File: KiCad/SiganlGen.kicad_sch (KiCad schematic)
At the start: 1 part, among them J1 Barrel_Jack_MountingPin

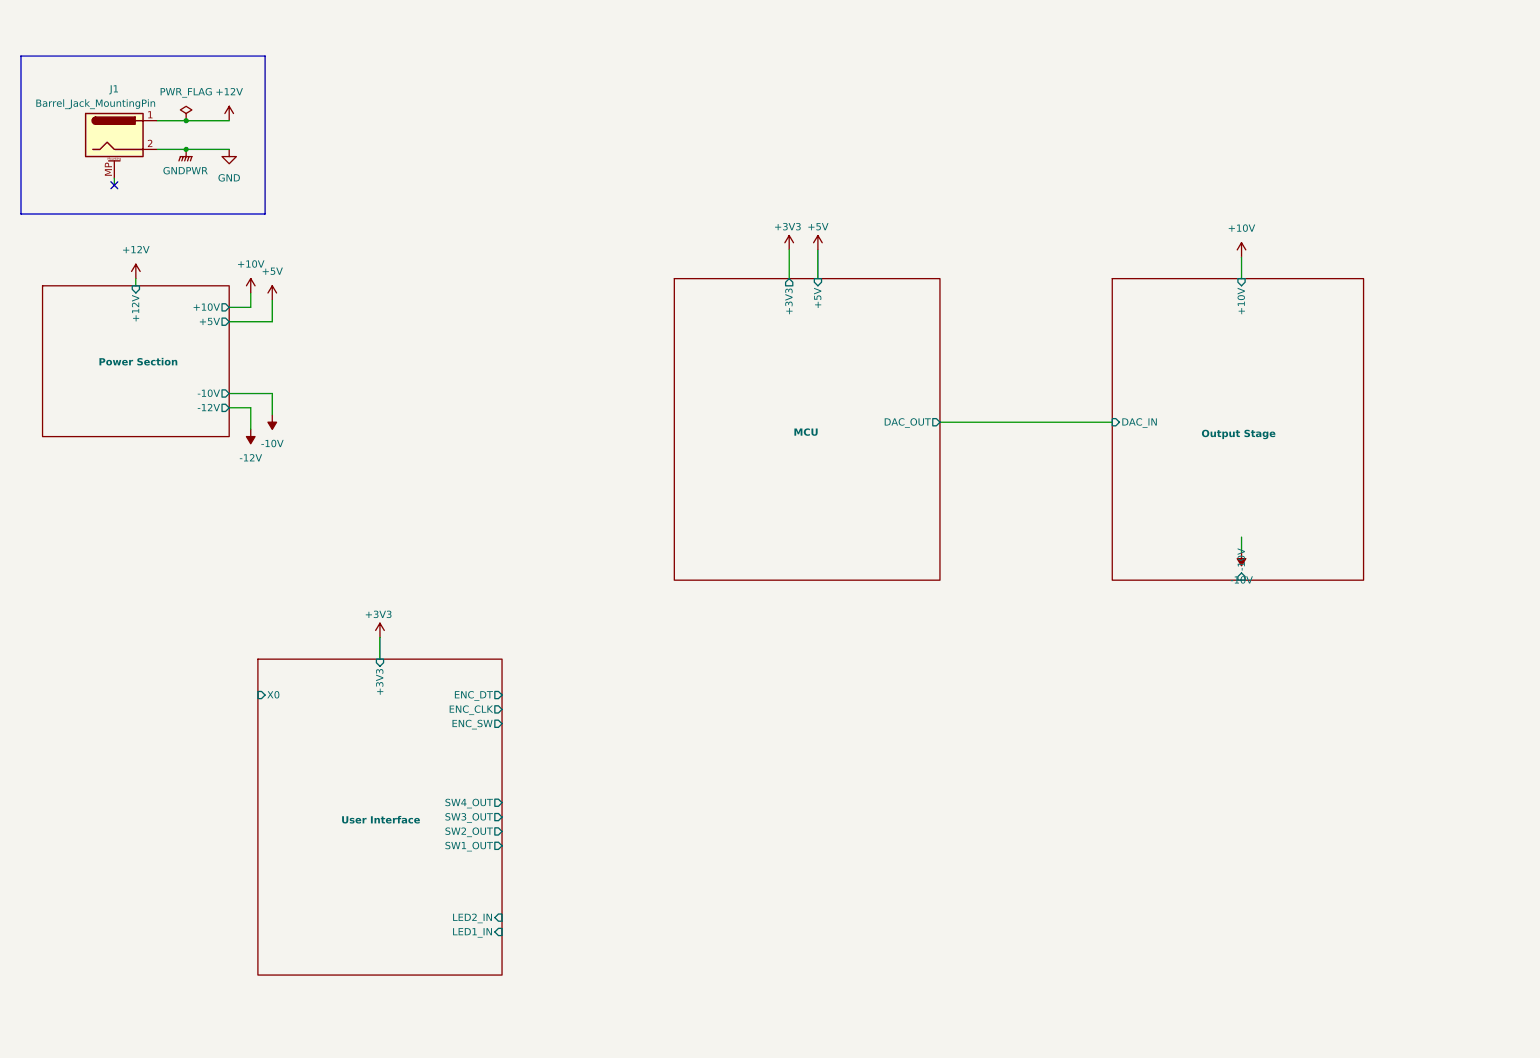
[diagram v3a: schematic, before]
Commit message: UI connections to uC
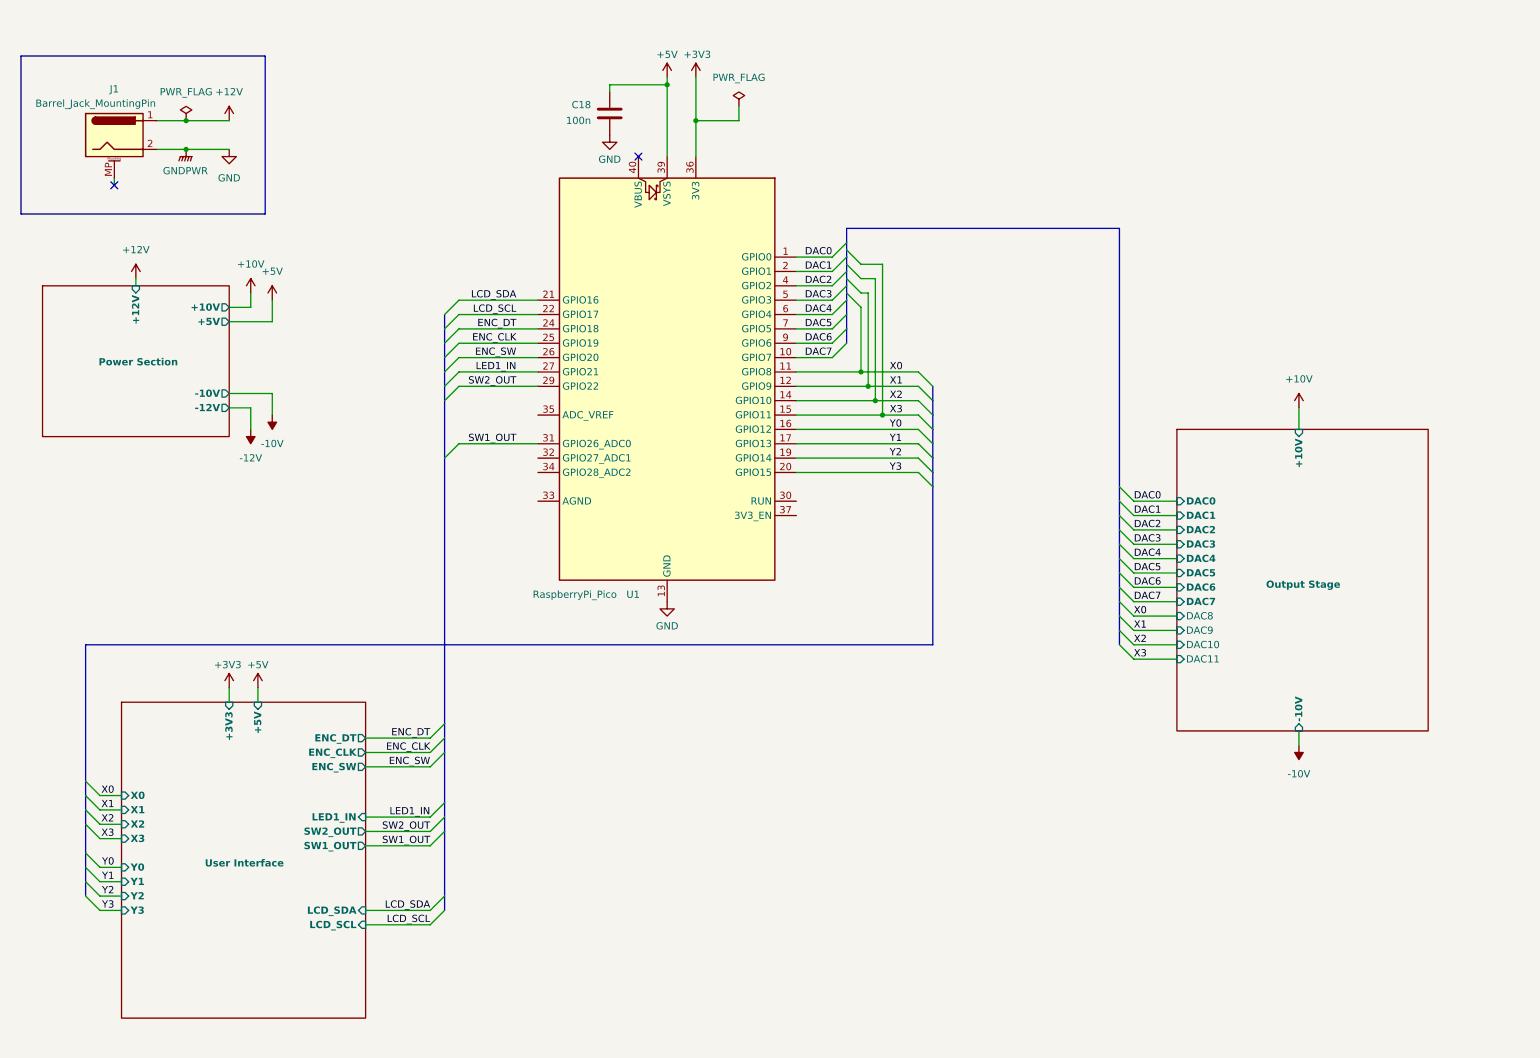
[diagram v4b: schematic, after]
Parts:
- added C18: 100n, Capacitor_SMD:C_0805_2012Metric_Pad1.18x1.45mm_HandSolder, symbol Device:C
- added U1: RaspberryPi_Pico, Module_RaspberryPi_Pico:RaspberryPi_Pico_Common, symbol MCU_Module_RaspberryPi_Pico:RaspberryPi_Pico
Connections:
- net +3V3: now also U1.36 (3V3)
- net +5V: now also C18.1, U1.39 (VSYS)
- net GND: now also C18.2, U1.13 (GND), U1.18 (GND), U1.23 (GND), U1.28 (GND), U1.3 (GND), U1.38 (GND), U1.8 (GND)
- new net DAC0: U1.1 (GPIO0)
- new net DAC1: U1.2 (GPIO1)
- new net DAC2: U1.4 (GPIO2)
- new net DAC3: U1.5 (GPIO3)
- new net DAC4: U1.6 (GPIO4)
- new net DAC5: U1.7 (GPIO5)
- new net DAC6: U1.9 (GPIO6)
- new net DAC7: U1.10 (GPIO7)
- new net ENC_CLK: U1.25 (GPIO19)
- new net ENC_DT: U1.24 (GPIO18)
- new net ENC_SW: U1.26 (GPIO20)
- new net LCD_SCL: U1.22 (GPIO17)
- new net LCD_SDA: U1.21 (GPIO16)
- new net LED1_IN: U1.27 (GPIO21)
- new net SW1_OUT: U1.31 (GPIO26_ADC0)
- new net SW2_OUT: U1.29 (GPIO22)
- new net X0: U1.11 (GPIO8)
- new net X1: U1.12 (GPIO9)
- new net X2: U1.14 (GPIO10)
- new net X3: U1.15 (GPIO11)
- new net Y0: U1.16 (GPIO12)
- new net Y1: U1.17 (GPIO13)
- new net Y2: U1.19 (GPIO14)
- new net Y3: U1.20 (GPIO15)
- no-connect marks 1 -> 2
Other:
- removed sheet MCU
- sheet Output Stage ports: added DAC0, DAC1, DAC10, DAC11, DAC2, DAC3, DAC4, DAC5, DAC6, DAC7, DAC8, DAC9; removed DAC_IN
- sheet User Interface ports: added +5V, LCD_SCL, LCD_SDA, X1, X2, X3, Y0, Y1, Y2, Y3; removed LED2_IN, SW3_OUT, SW4_OUT

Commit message: First DAC layout, rough board layout
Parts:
- renumbered C18 to C1
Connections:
- net GND: now also J1.MP (MountPin)
- no-connect marks 2 -> 1
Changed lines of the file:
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@@
 	)
 	(junction
+		(at 40.64 36.83)
+		(diameter 0)
+		(color 0 0 0 0)
+	)
+	(junction
 		(at 45.72 36.83)
 		(diameter 0)
@@
 		(at 125.73 38.1)
 	)
-	(no_connect
-		(at 33.02 43.18)
-	)
 	(bus_entry
 		(at 162.56 62.23)
@@
 	(wire
 		(pts
+			(xy 33.02 43.18) (xy 33.02 41.91)
+		)
+		(stroke
+			(width 0)
+			(type default)
+		)
+	)
+	(wire
+		(pts
 			(xy 213.36 124.46) (xy 220.98 124.46)
 		)
@@
 		)
 	)
-	(wire
-		(pts
-			(xy 33.02 43.18) (xy 33.02 41.91)
-		)
-		(stroke
-			(width 0)
-			(type default)
-		)
-	)
 	(bus
 		(pts
@@
 	(wire
 		(pts
+			(xy 40.64 36.83) (xy 40.64 43.18)
+		)
+		(stroke
+			(width 0)
+			(type default)
+		)
+	)
+	(wire
+		(pts
 			(xy 166.37 78.74) (xy 175.26 78.74)
 		)
@@
 	(wire
 		(pts
+			(xy 33.02 43.18) (xy 40.64 43.18)
+		)
+		(stroke
+			(width 0)
+			(type default)
+		)
+	)
+	(wire
+		(pts
 			(xy 213.36 104.14) (xy 220.98 104.14)
 		)
@@
 		(dnp no)
 		(fields_autoplaced yes)
-		(property "Reference" "#PWR05"
+		(property "Reference" "#PWR018"
 			(at 60.96 67.31 0)
 			(effects
@@
 			(project "SiganlGen"
 				(path "/e2db369b-fed9-4358-b449-15db5155edf2"
-					(reference "#PWR05")
+					(reference "#PWR018")
 					(unit 1)
 				)
@@
 		(dnp no)
 		(fields_autoplaced yes)
-		(property "Reference" "#PWR03"
+		(property "Reference" "#PWR02"
 			(at 45.72 41.91 0)
 			(effects
@@
 			(project "SiganlGen"
 				(path "/e2db369b-fed9-4358-b449-15db5155edf2"
-					(reference "#PWR03")
+					(reference "#PWR02")
 					(unit 1)
 				)
@@
 		(dnp no)
 		(fields_autoplaced yes)
-		(property "Reference" "#PWR04"
+		(property "Reference" "#PWR06"
 			(at 57.15 66.04 0)
 			(effects
@@
 			(project "SiganlGen"
 				(path "/e2db369b-fed9-4358-b449-15db5155edf2"
-					(reference "#PWR04")
+					(reference "#PWR06")
 					(unit 1)
 				)
@@
 		(on_board yes)
 		(dnp no)
-		(property "Reference" "#PWR032"
+		(property "Reference" "#PWR028"
 			(at 135.89 27.94 0)
 			(effects
@@
 			(project "SiganlGen"
 				(path "/e2db369b-fed9-4358-b449-15db5155edf2"
-					(reference "#PWR032")
+					(reference "#PWR028")
 					(unit 1)
 				)
@@
 		(dnp no)
 		(fields_autoplaced yes)
-		(property "Reference" "#PWR010"
+		(property "Reference" "#PWR020"
 			(at 60.96 80.01 0)
 			(effects
@@
 			(project "SiganlGen"
 				(path "/e2db369b-fed9-4358-b449-15db5155edf2"
-					(reference "#PWR010")
+					(reference "#PWR020")
 					(unit 1)
 				)
@@
 		(dnp no)
 		(fields_autoplaced yes)
-		(property "Reference" "#PWR022"
+		(property "Reference" "#PWR01"
 			(at 36.83 63.5 0)
 			(effects
@@
 			(project "SiganlGen"
 				(path "/e2db369b-fed9-4358-b449-15db5155edf2"
-					(reference "#PWR022")
+					(reference "#PWR01")
 					(unit 1)
 				)
@@
 		(dnp no)
 		(fields_autoplaced yes)
-		(property "Reference" "#PWR01"
+		(property "Reference" "#PWR03"
 			(at 53.34 35.56 0)
 			(effects
@@
 			(project "SiganlGen"
 				(path "/e2db369b-fed9-4358-b449-15db5155edf2"
-					(reference "#PWR01")
+					(reference "#PWR03")
 					(unit 1)
 				)
@@
 		(on_board yes)
 		(dnp no)
-		(property "Reference" "#PWR023"
+		(property "Reference" "#PWR05"
 			(at 53.34 135.89 0)
 			(effects
@@
 			(project "SiganlGen"
 				(path "/e2db369b-fed9-4358-b449-15db5155edf2"
-					(reference "#PWR023")
+					(reference "#PWR05")
 					(unit 1)
 				)
@@
 		(on_board yes)
 		(dnp no)
-		(property "Reference" "#PWR033"
+		(property "Reference" "#PWR022"
 			(at 130.81 27.94 0)
 			(effects
@@
 			(project "SiganlGen"
 				(path "/e2db369b-fed9-4358-b449-15db5155edf2"
-					(reference "#PWR033")
+					(reference "#PWR022")
 					(unit 1)
 				)
@@
 		(on_board yes)
 		(dnp no)
-		(property "Reference" "#PWR020"
+		(property "Reference" "#PWR023"
 			(at 130.81 123.19 0)
 			(effects
@@
 			(project "SiganlGen"
 				(path "/e2db369b-fed9-4358-b449-15db5155edf2"
-					(reference "#PWR020")
+					(reference "#PWR023")
 					(unit 1)
 				)
@@
 		(dnp no)
 		(fields_autoplaced yes)
-		(property "Reference" "#PWR021"
+		(property "Reference" "#PWR030"
 			(at 242.57 86.36 0)
 			(effects
@@
 			(project "SiganlGen"
 				(path "/e2db369b-fed9-4358-b449-15db5155edf2"
-					(reference "#PWR021")
+					(reference "#PWR030")
 					(unit 1)
 				)
@@
 		(dnp no)
 		(fields_autoplaced yes)
-		(property "Reference" "#PWR018"
+		(property "Reference" "#PWR031"
 			(at 242.57 138.43 0)
 			(effects
@@
 			(project "SiganlGen"
 				(path "/e2db369b-fed9-4358-b449-15db5155edf2"
-					(reference "#PWR018")
+					(reference "#PWR031")
 					(unit 1)
 				)
@@
 		(on_board yes)
 		(dnp no)
-		(property "Reference" "#PWR011"
+		(property "Reference" "#PWR021"
 			(at 120.65 40.64 0)
 			(effects
@@
 			(project "SiganlGen"
 				(path "/e2db369b-fed9-4358-b449-15db5155edf2"
-					(reference "#PWR011")
+					(reference "#PWR021")
 					(unit 1)
 				)
@@
 		(dnp no)
 		(fields_autoplaced yes)
-		(property "Reference" "#PWR06"
+		(property "Reference" "#PWR010"
 			(at 57.15 82.55 0)
 			(effects
@@
 			(project "SiganlGen"
 				(path "/e2db369b-fed9-4358-b449-15db5155edf2"
-					(reference "#PWR06")
+					(reference "#PWR010")
 					(unit 1)
 				)
@@
 		(on_board yes)
 		(dnp no)
-		(property "Reference" "C18"
+		(property "Reference" "C1"
 			(at 117.348 28.956 0)
 			(effects
@@
 			(project "SiganlGen"
 				(path "/e2db369b-fed9-4358-b449-15db5155edf2"
-					(reference "C18")
+					(reference "C1")
 					(unit 1)
 				)
@@
 		(on_board yes)
 		(dnp no)
-		(property "Reference" "#PWR028"
+		(property "Reference" "#PWR011"
 			(at 58.42 135.89 0)
 			(effects
@@
 			(project "SiganlGen"
 				(path "/e2db369b-fed9-4358-b449-15db5155edf2"
-					(reference "#PWR028")
+					(reference "#PWR011")
 					(unit 1)
 				)
@@
 		(dnp no)
 		(fields_autoplaced yes)
-		(property "Reference" "#PWR02"
+		(property "Reference" "#PWR04"
 			(at 53.34 43.18 0)
 			(effects
@@
 			(project "SiganlGen"
 				(path "/e2db369b-fed9-4358-b449-15db5155edf2"
-					(reference "#PWR02")
+					(reference "#PWR04")
 					(unit 1)
 				)

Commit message: minor changes, testing
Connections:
- no-connect marks 1 -> 7

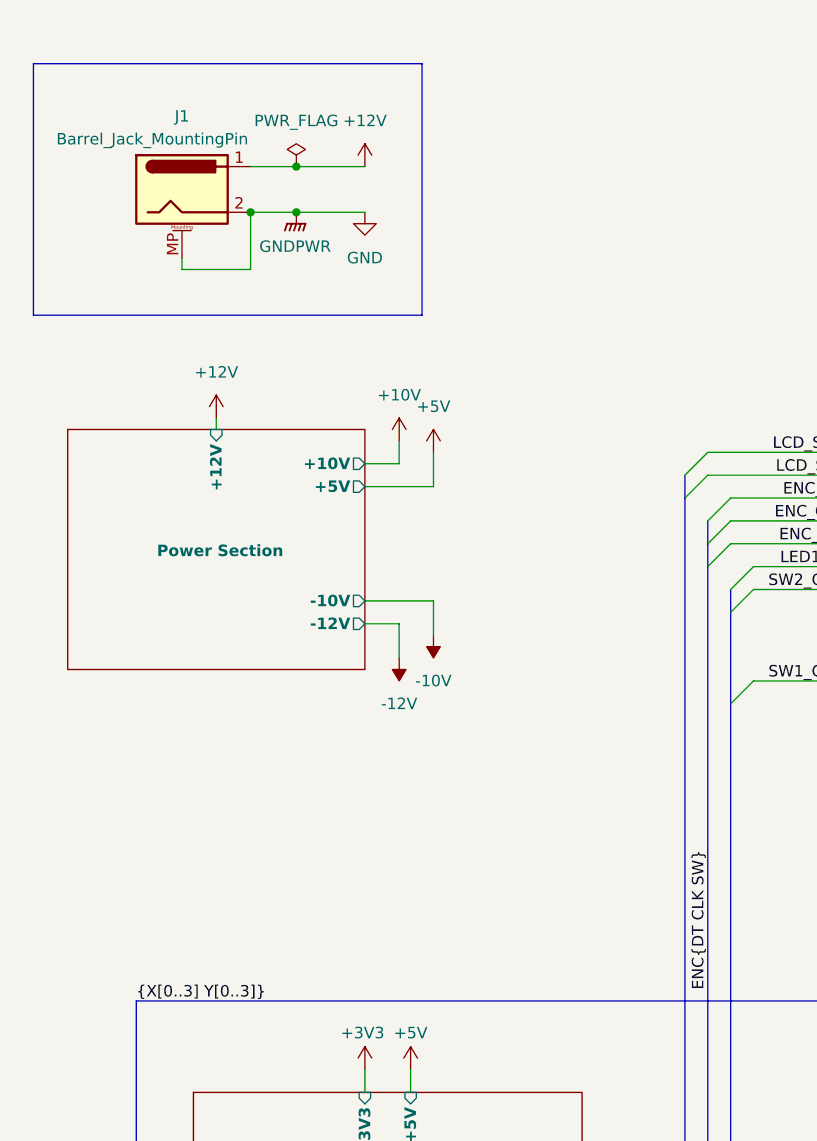
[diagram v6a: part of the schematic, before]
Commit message: Added protection elements and an additional input connector
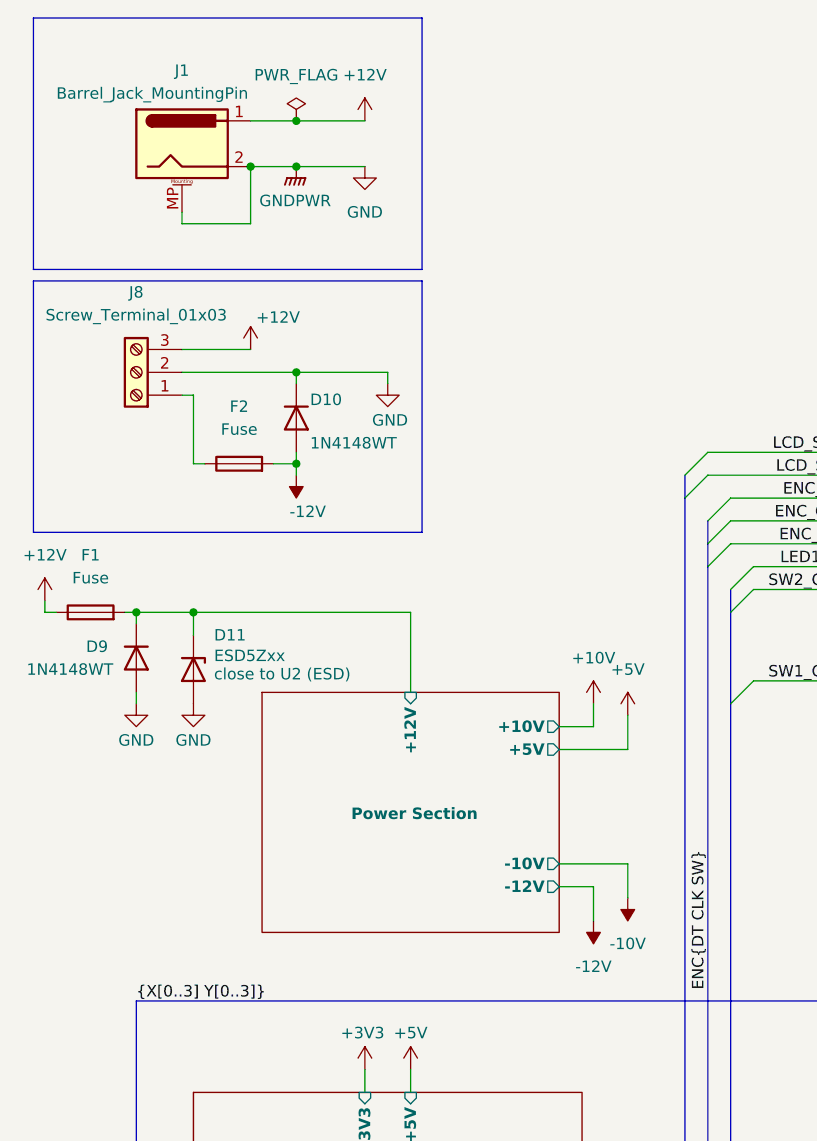
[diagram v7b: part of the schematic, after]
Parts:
- added D10, D9: 1N4148WT, Diode_SMD:D_SOD-523, symbol Diode:1N4148WT
- added D11: ESD5Zxx, Diode_SMD:D_SOD-523, symbol Diode:ESD5Zxx
- added F1, F2: Fuse, symbol Device:Fuse
- added J8: Screw_Terminal_01x03, symbol Connector:Screw_Terminal_01x03
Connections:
- net +12V: now also F1.1, J8.3 (Pin_3)
- net -12V: now also D10.2 (A), F2.2
- net GND: now also D10.1 (K), D11.2 (A), D9.2 (A), J8.2 (Pin_2)
- new net: F2.1, J8.1 (Pin_1)
- new net Power Section/+12V: D11.1 (K), D9.1 (K), F1.2
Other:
- moved on the sheet: J1

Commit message: Added/changed footprints
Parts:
- F1, F2: footprint (none) -> Fuse:Fuseholder_Clip-5x20mm_Keystone_3517_Inline_P23.11x6.76mm_D1.70mm_Horizontal
- J8: footprint (none) -> TerminalBlock_MetzConnect:TerminalBlock_MetzConnect_Type094_RT03503HBLU_1x03_P5.00mm_Horizontal
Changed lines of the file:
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@@
 			)
 		)
-		(property "Footprint" ""
+		(property "Footprint" "Fuse:Fuseholder_Clip-5x20mm_Keystone_3517_Inline_P23.11x6.76mm_D1.70mm_Horizontal"
 			(at 22.86 83.058 90)
 			(effects
@@
 			)
 		)
-		(property "Footprint" ""
+		(property "Footprint" "TerminalBlock_MetzConnect:TerminalBlock_MetzConnect_Type094_RT03503HBLU_1x03_P5.00mm_Horizontal"
 			(at 27.94 54.61 0)
 			(effects
@@
 			)
 		)
-		(property "Footprint" ""
+		(property "Footprint" "Fuse:Fuseholder_Clip-5x20mm_Keystone_3517_Inline_P23.11x6.76mm_D1.70mm_Horizontal"
 			(at 39.37 66.548 90)
 			(effects
